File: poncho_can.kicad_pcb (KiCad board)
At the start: 2 copper layers, 85.7 x 60.3 mm, 33 parts, among them J10 GS2, J101 DB9_Male_MountingHoles, J102 DB9_Male_MountingHoles, J103 GS2, J104 GS2, J105 GS2, J106 GS2, J7 GS2, J8 GS2, J9 GS2, U101 TJA1051T, U102 TJA1051T

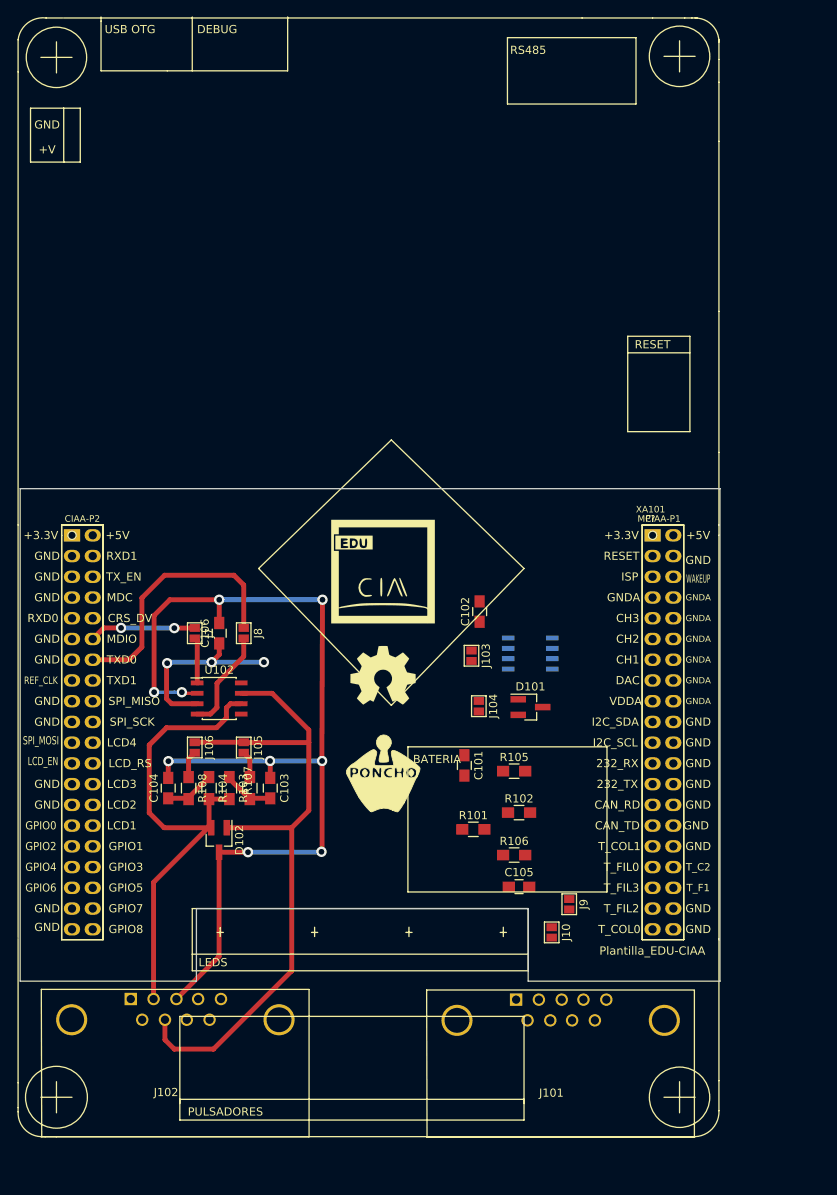
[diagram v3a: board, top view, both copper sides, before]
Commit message: Nueva colocación de los componentes
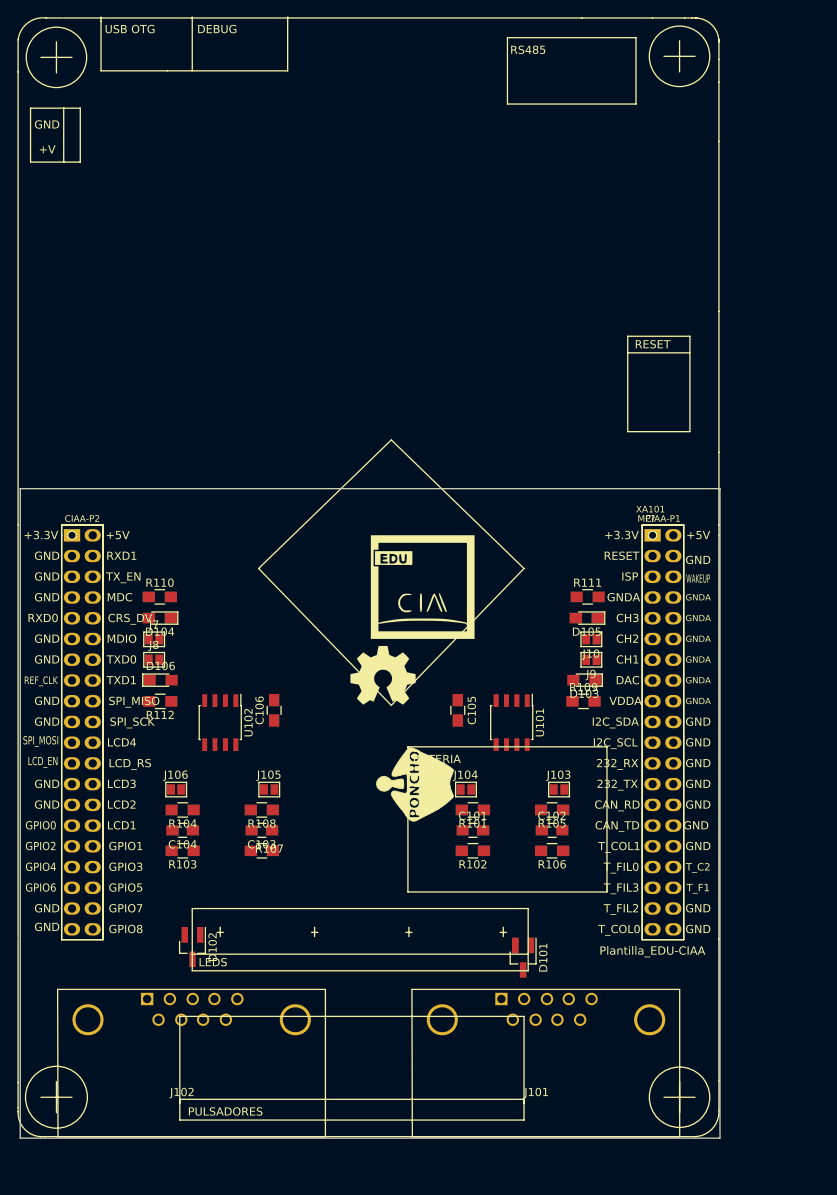
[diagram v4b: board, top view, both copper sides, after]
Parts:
- added D103: LED_RX, LEDs:LED_0805_HandSoldering, F.Cu at (128.8, 104.1)
- added D104: LED_TX, LEDs:LED_0805_HandSoldering, F.Cu at (76.8, 96.5)
- added D105: LED_TX, LEDs:LED_0805_HandSoldering, F.Cu at (129.1, 96.5)
- added D106: LED_RX, LEDs:LED_0805_HandSoldering, F.Cu at (76.9, 104.1)
- added R109: 270, Resistors_SMD:R_0805_HandSoldering, F.Cu at (128.7, 106.7)
- added R110: 270, Resistors_SMD:R_0805_HandSoldering, F.Cu at (76.8, 93.9)
- added R111: 270, Resistors_SMD:R_0805_HandSoldering, F.Cu at (129.2, 93.9)
- added R112: 270, Resistors_SMD:R_0805_HandSoldering, F.Cu at (76.8, 106.7)
- U101: moved to F.Cu
- moved J10 36.2 mm to (129.7, 99.1), turned to 270 degrees
- moved D101 30.7 mm to (121.3, 138.1), turned to 270 degrees
- moved J9 30.1 mm to (129.7, 101.6), turned to 270 degrees
- moved C102 28.2 mm to (124.8, 122.5), turned to 0 degrees
- moved C105 22.9 mm to (113.3, 107.8), turned to 270 degrees
- moved J103 19.6 mm to (125.7, 117.5), turned to 90 degrees
- moved D102 13.5 mm to (80.8, 136.8)
- moved C106 11.6 mm to (90.8, 107.8)
- moved J8 11.4 mm to (76.1, 101.6), turned to 90 degrees
- moved J104 10.3 mm to (114.3, 117.5), turned to 90 degrees
- moved R103 9.58 mm to (79.6, 125.0), turned to 180 degrees
- moved R108 9.37 mm to (89.3, 120.0), turned to 180 degrees
- moved U101 8.76 mm to (119.9, 109.3), turned to 270 degrees
- moved C101 8.02 mm to (115.2, 122.5), turned to 0 degrees
- moved R107 7.82 mm to (89.3, 125.0), turned to 180 degrees
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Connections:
- J101 pad 1: Net-(J101-Pad1) -> (no net)
- J101 pad 4: Net-(J101-Pad4) -> (no net)
- J101 pad 5: Net-(J101-Pad5) -> (no net)
- J101 pad 6: Net-(J101-Pad6) -> (no net)
- J101 pad 8: Net-(J101-Pad8) -> (no net)
- J101 pad 9: Net-(J101-Pad9) -> (no net)
- J102 pad 1: Net-(J102-Pad1) -> (no net)
- J102 pad 4: Net-(J102-Pad4) -> (no net)
- J102 pad 5: Net-(J102-Pad5) -> (no net)
- J102 pad 6: Net-(J102-Pad6) -> (no net)
- J102 pad 8: Net-(J102-Pad8) -> (no net)
- J102 pad 9: Net-(J102-Pad9) -> (no net)
- J104 pad 1: Net-(D101-Pad1) -> Net-(J104-Pad1)
- J104 pad 2: Net-(J104-Pad2) -> Net-(D101-Pad2)
- J106 pad 1: Net-(D102-Pad1) -> Net-(J106-Pad1)
- J106 pad 2: Net-(J106-Pad2) -> Net-(D102-Pad2)
- R101 pad 2: Net-(D101-Pad2) -> Net-(J104-Pad1)
- R102 pad 2: Net-(D101-Pad2) -> Net-(J104-Pad1)
- R103 pad 2: Net-(D102-Pad2) -> Net-(J106-Pad1)
- R104 pad 2: Net-(D102-Pad2) -> Net-(J106-Pad1)
- R106 pad 1: Net-(J104-Pad2) -> Net-(J103-Pad2)
- R108 pad 1: Net-(J106-Pad2) -> Net-(J105-Pad2)
- U101 pad 5: Net-(U101-Pad5) -> (no net)
- U101 pad 8: Net-(U101-Pad8) -> (no net)
- U102 pad 5: Net-(U102-Pad5) -> (no net)
- U102 pad 8: Net-(U102-Pad8) -> (no net)
- XA101 pad 1: +3V3 -> +3.3VP
- XA101 pad 11: Net-(XA101-Pad11) -> (no net)
- XA101 pad 13: Net-(XA101-Pad13) -> (no net)
- XA101 pad 15: Net-(XA101-Pad15) -> (no net)
- XA101 pad 17: Net-(XA101-Pad17) -> (no net)
- XA101 pad 19: Net-(XA101-Pad19) -> (no net)
- XA101 pad 21: Net-(XA101-Pad21) -> (no net)
- XA101 pad 23: Net-(XA101-Pad23) -> (no net)
- XA101 pad 25: Net-(XA101-Pad25) -> (no net)
- XA101 pad 3: Net-(XA101-Pad3) -> (no net)
- XA101 pad 31: Net-(XA101-Pad31) -> (no net)
- XA101 pad 33: Net-(XA101-Pad33) -> (no net)
- XA101 pad 34: Net-(XA101-Pad34) -> (no net)
- XA101 pad 35: Net-(XA101-Pad35) -> (no net)
- XA101 pad 36: Net-(XA101-Pad36) -> (no net)
- XA101 pad 37: Net-(XA101-Pad37) -> (no net)
- XA101 pad 39: Net-(XA101-Pad39) -> (no net)
- XA101 pad 42: +5VP -> +5V
- XA101 pad 43: GNDD -> GND
- XA101 pad 44: Net-(XA101-Pad44) -> (no net)
- XA101 pad 45: GNDD -> GND
- XA101 pad 46: Net-(XA101-Pad46) -> (no net)
- XA101 pad 47: GNDD -> GND
- XA101 pad 48: Net-(XA101-Pad48) -> (no net)
- XA101 pad 49: Net-(XA101-Pad49) -> (no net)
- XA101 pad 5: Net-(XA101-Pad5) -> (no net)
- XA101 pad 50: Net-(XA101-Pad50) -> (no net)
- XA101 pad 51: GNDD -> GND
- XA101 pad 53: GNDD -> GND
- XA101 pad 55: Net-(XA101-Pad55) -> (no net)
- XA101 pad 56: Net-(XA101-Pad56) -> (no net)
- XA101 pad 57: GNDD -> GND
- XA101 pad 58: Net-(XA101-Pad58) -> (no net)
- XA101 pad 59: GNDD -> GND
- XA101 pad 6: Net-(XA101-Pad6) -> (no net)
- XA101 pad 60: Net-(XA101-Pad60) -> (no net)
- XA101 pad 61: Net-(XA101-Pad61) -> (no net)
- XA101 pad 62: Net-(XA101-Pad62) -> (no net)
- XA101 pad 63: Net-(XA101-Pad63) -> (no net)
- XA101 pad 64: Net-(XA101-Pad64) -> (no net)
- XA101 pad 65: GNDD -> GND
- XA101 pad 66: Net-(XA101-Pad66) -> (no net)
- XA101 pad 67: GNDD -> GND
- XA101 pad 68: Net-(XA101-Pad68) -> (no net)
- XA101 pad 69: Net-(XA101-Pad69) -> (no net)
- XA101 pad 70: Net-(XA101-Pad70) -> (no net)
- XA101 pad 71: Net-(XA101-Pad71) -> (no net)
- XA101 pad 72: Net-(XA101-Pad72) -> (no net)
- XA101 pad 73: Net-(XA101-Pad73) -> (no net)
- XA101 pad 74: Net-(XA101-Pad74) -> (no net)
- XA101 pad 75: Net-(XA101-Pad75) -> (no net)
- XA101 pad 76: Net-(XA101-Pad76) -> (no net)
- XA101 pad 77: GNDD -> GND
- XA101 pad 78: Net-(XA101-Pad78) -> (no net)
- XA101 pad 79: GNDD -> GND
- XA101 pad 80: Net-(XA101-Pad80) -> (no net)
- XA101 pad 9: Net-(XA101-Pad9) -> (no net)
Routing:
- net GND: track 125.6 -> 0.00 mm, vias 9 -> 0
- net Net-(D102-Pad1): track 85.3 -> 0.00 mm
- net Net-(D102-Pad2): track 61.0 -> 0.00 mm
- net Net-(D106-Pad1): track 32.1 -> 0.00 mm
- net +5V: track 23.0 -> 0.00 mm, vias 3 -> 0
- net Net-(D104-Pad1): track 13.1 -> 0.00 mm, vias 2 -> 0
- net Net-(J8-Pad2): track 12.6 -> 0.00 mm
- net Net-(C103-Pad2): track 6.28 -> 0.00 mm
- net Net-(C104-Pad1): track 6.28 -> 0.00 mm
- net Net-(J7-Pad2): track 5.58 -> 0.00 mm
- net Net-(J106-Pad2): track 3.30 -> 0.00 mm
- net Net-(J105-Pad2): track 3.30 -> 0.00 mm
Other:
- board size 85.7 x 60.3 mm -> 85.7 x 79.6 mm
- rule pad_to_mask_clearance: 0.2 -> 0.05

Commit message: Ruteo de los componentes
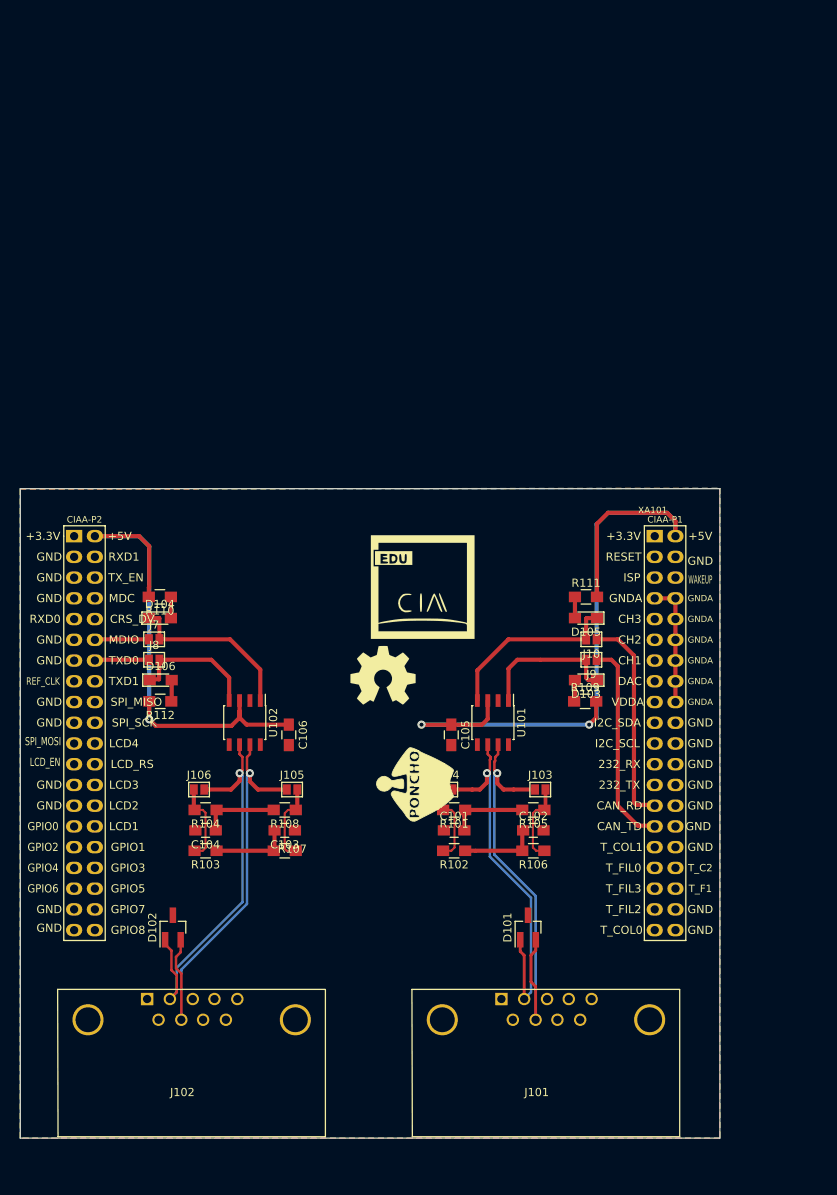
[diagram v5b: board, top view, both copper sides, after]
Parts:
- removed MP?: Plantilla_EDU-CIAA, footprint:Plantilla_EDU-CIAA
- moved D101 3.75 mm to (121.9, 134.4), turned to 90 degrees
- moved C106 3.50 mm to (92.6, 110.8), turned to 270 degrees
- moved D102 3.39 mm to (78.4, 134.4), turned to 90 degrees
- moved C105 3.10 mm to (112.5, 110.8)
- moved U102 3.00 mm to (87.2, 109.3)
- moved C104 2.80 mm to (82.4, 122.5)
- moved R103 2.80 mm to (82.4, 125.0)
- moved R104 2.80 mm to (82.4, 120.0)
- moved C103 2.80 mm to (92.1, 122.5)
- moved J105 2.80 mm to (93.0, 117.5)
- moved J106 2.80 mm to (81.6, 117.5)
- moved R107 2.80 mm to (92.1, 125.0)
- moved R108 2.80 mm to (92.1, 120.0)
- moved C101 2.30 mm to (112.8, 122.5)
- moved R101 2.30 mm to (112.8, 120.0)
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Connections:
- C106 pad 1: +5V -> +5VP
- D101 pad 1: Net-(D101-Pad1) -> /CAN1-
- D101 pad 2: Net-(D101-Pad2) -> /CAN1+
- D102 pad 1: Net-(D102-Pad1) -> /CAN2-
- D102 pad 2: Net-(D102-Pad2) -> /CAN2+
- J10 pad 1: Net-(D105-Pad1) -> Net-(J10-Pad1)
- J10 pad 2: Net-(J10-Pad2) -> Net-(D105-Pad1)
- J101 pad 2: Net-(D101-Pad2) -> /CAN1-
- J101 pad 7: Net-(D101-Pad1) -> /CAN1+
- J102 pad 2: Net-(D102-Pad2) -> /CAN2-
- J102 pad 7: Net-(D102-Pad1) -> /CAN2+
- J103 pad 1: Net-(D101-Pad1) -> /CAN1+
- J104 pad 2: Net-(D101-Pad2) -> /CAN1-
- J105 pad 1: Net-(D102-Pad1) -> /CAN2+
- J106 pad 2: Net-(D102-Pad2) -> /CAN2-
- J7 pad 1: Net-(D104-Pad1) -> Net-(J7-Pad1)
- J7 pad 2: Net-(J7-Pad2) -> Net-(D104-Pad1)
- J8 pad 1: Net-(D106-Pad1) -> Net-(J8-Pad1)
- J8 pad 2: Net-(J8-Pad2) -> Net-(D106-Pad1)
- J9 pad 1: Net-(D103-Pad1) -> Net-(J9-Pad1)
- J9 pad 2: Net-(J9-Pad2) -> Net-(D103-Pad1)
- R110 pad 2: +5V -> +5VP
- R112 pad 2: +5V -> +5VP
- U101 pad 1: Net-(J9-Pad2) -> Net-(D103-Pad1)
- U101 pad 4: Net-(J10-Pad2) -> Net-(D105-Pad1)
- U101 pad 6: Net-(D101-Pad2) -> /CAN1-
- U101 pad 7: Net-(D101-Pad1) -> /CAN1+
- U102 pad 1: Net-(J7-Pad2) -> Net-(D104-Pad1)
- U102 pad 3: +5V -> +5VP
- U102 pad 4: Net-(J8-Pad2) -> Net-(D106-Pad1)
- U102 pad 6: Net-(D102-Pad2) -> /CAN2-
- U102 pad 7: Net-(D102-Pad1) -> /CAN2+
- XA101 pad 1: +3.3VP -> (no net)
- XA101 pad 27: Net-(D105-Pad1) -> Net-(J10-Pad1)
- XA101 pad 29: Net-(D103-Pad1) -> Net-(J9-Pad1)
- XA101 pad 41: +3.3VP -> (no net)
- XA101 pad 42: +5V -> +5VP
- XA101 pad 52: Net-(D104-Pad1) -> Net-(J7-Pad1)
- XA101 pad 54: Net-(D106-Pad1) -> Net-(J8-Pad1)
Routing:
- net +5V: track 0.00 -> 93.2 mm, vias 0 -> 2
- net +5VP: track 0.00 -> 65.1 mm, vias 0 -> 1
- net /CAN2+: track 0.00 -> 53.7 mm, vias 0 -> 1
- net /CAN1+: track 0.00 -> 52.7 mm, vias 0 -> 1
- net /CAN2-: track 0.00 -> 49.2 mm, vias 0 -> 1
- net /CAN1-: track 0.00 -> 47.3 mm, vias 0 -> 1
- net Net-(J10-Pad1): track 0.00 -> 25.8 mm
- net Net-(J9-Pad1): track 0.00 -> 25.3 mm
- net Net-(D105-Pad1): track 0.00 -> 22.5 mm
- net Net-(D104-Pad1): track 0.00 -> 21.6 mm
- net Net-(D103-Pad1): track 0.00 -> 17.3 mm
- net Net-(D106-Pad1): track 0.00 -> 15.9 mm
- net GNDA: track 0.00 -> 15.2 mm
- net Net-(J105-Pad2): track 0.00 -> 10.0 mm
- net Net-(J106-Pad1): track 0.00 -> 9.83 mm
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- added copper zone on B.Cu, net GND
- added copper zone on F.Cu, net GND
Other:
- net class Default: clearance 0.4 -> 0.254; trace_width 0.6 -> 0.1524; via_dia 1.27 -> 1; via_drill 0.7 -> 0.5
- rule trace_clearance: 0.4 -> 0.254
- rule trace_min: 0.4 -> 0.1524
- rule via_min_drill: 0.3 -> 0.4064
- rule via_min_size: 0.4 -> 0.7112

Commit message: Fin de esquematico y agrego los gerbers
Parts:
- moved G*** 33.8 mm to (108.8, 83.1), turned to 0 degrees
- moved C105 30.8 mm to (128.6, 84.5)
- moved D104 28.1 mm to (86.9, 70.2)
- moved J7 28.1 mm to (86.2, 72.8)
- moved J8 28.1 mm to (86.2, 75.3)
- moved R110 28.1 mm to (86.9, 67.7)
- moved R112 28.1 mm to (87.0, 80.5)
- moved D106 28.1 mm to (87.0, 77.8)
- moved G*** 28.0 mm to (108.8, 64.8)
- moved C101 26.9 mm to (119.0, 96.2)
- moved C102 26.9 mm to (128.7, 96.2)
- moved C103 26.9 mm to (98.2, 96.2)
- moved C106 26.9 mm to (98.7, 84.5)
- moved J106 26.9 mm to (87.7, 91.2)
- moved R101 26.9 mm to (119.0, 93.8)
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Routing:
- net GNDA: track 15.2 -> 38.1 mm
- net +5V: track 93.2 -> 82.0 mm, vias 2 -> 1
- net Net-(D105-Pad1): track 22.5 -> 17.8 mm
- net Net-(D103-Pad1): track 17.3 -> 12.9 mm
- net Net-(D106-Pad1): track 15.9 -> 11.8 mm
- net Net-(D104-Pad1): track 21.6 -> 17.5 mm
- net +5VP: track 65.1 -> 69.1 mm
- net Net-(J7-Pad1): track 6.64 -> 10.6 mm
- net Net-(J8-Pad1): track 6.66 -> 10.7 mm
- net Net-(J9-Pad1): track 25.3 -> 28.7 mm
- net Net-(J10-Pad1): track 25.8 -> 29.1 mm
- net /CAN1-: track 47.3 -> 50.2 mm
- net /CAN2-: track 49.2 -> 52.0 mm
- net Net-(J104-Pad1): track 7.34 -> 9.89 mm
- net /CAN2+: track 53.7 -> 55.7 mm
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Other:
- net class Default: clearance 0.254 -> 0.1524
- rule trace_clearance: 0.254 -> 0.1524
- board text added: "LB"
- board text added: "LT"
- board text added: "PONCHO CAN http://www.proyecto-ciaa.com.ar/"
- board text removed: "Borrar (Footprint MP1) la Plantilla-EDU-CIAA al finalizar el posicionamiento y definido el borde de PCB."
- board text removed: "PONCHO BASICO http://www.proyecto-ciaa.com.ar/"
- board text removed: "Se sugiere colocar Nombre de Poncho y autor en cobre, serigrafía y rótulo."
